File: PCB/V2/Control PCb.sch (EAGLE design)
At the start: 31 parts, among them Q1 DMP2305U-7, Q2 BSS123, Q3 BSS123, U1 V_REG_317DPACK, U2 5ACFEW

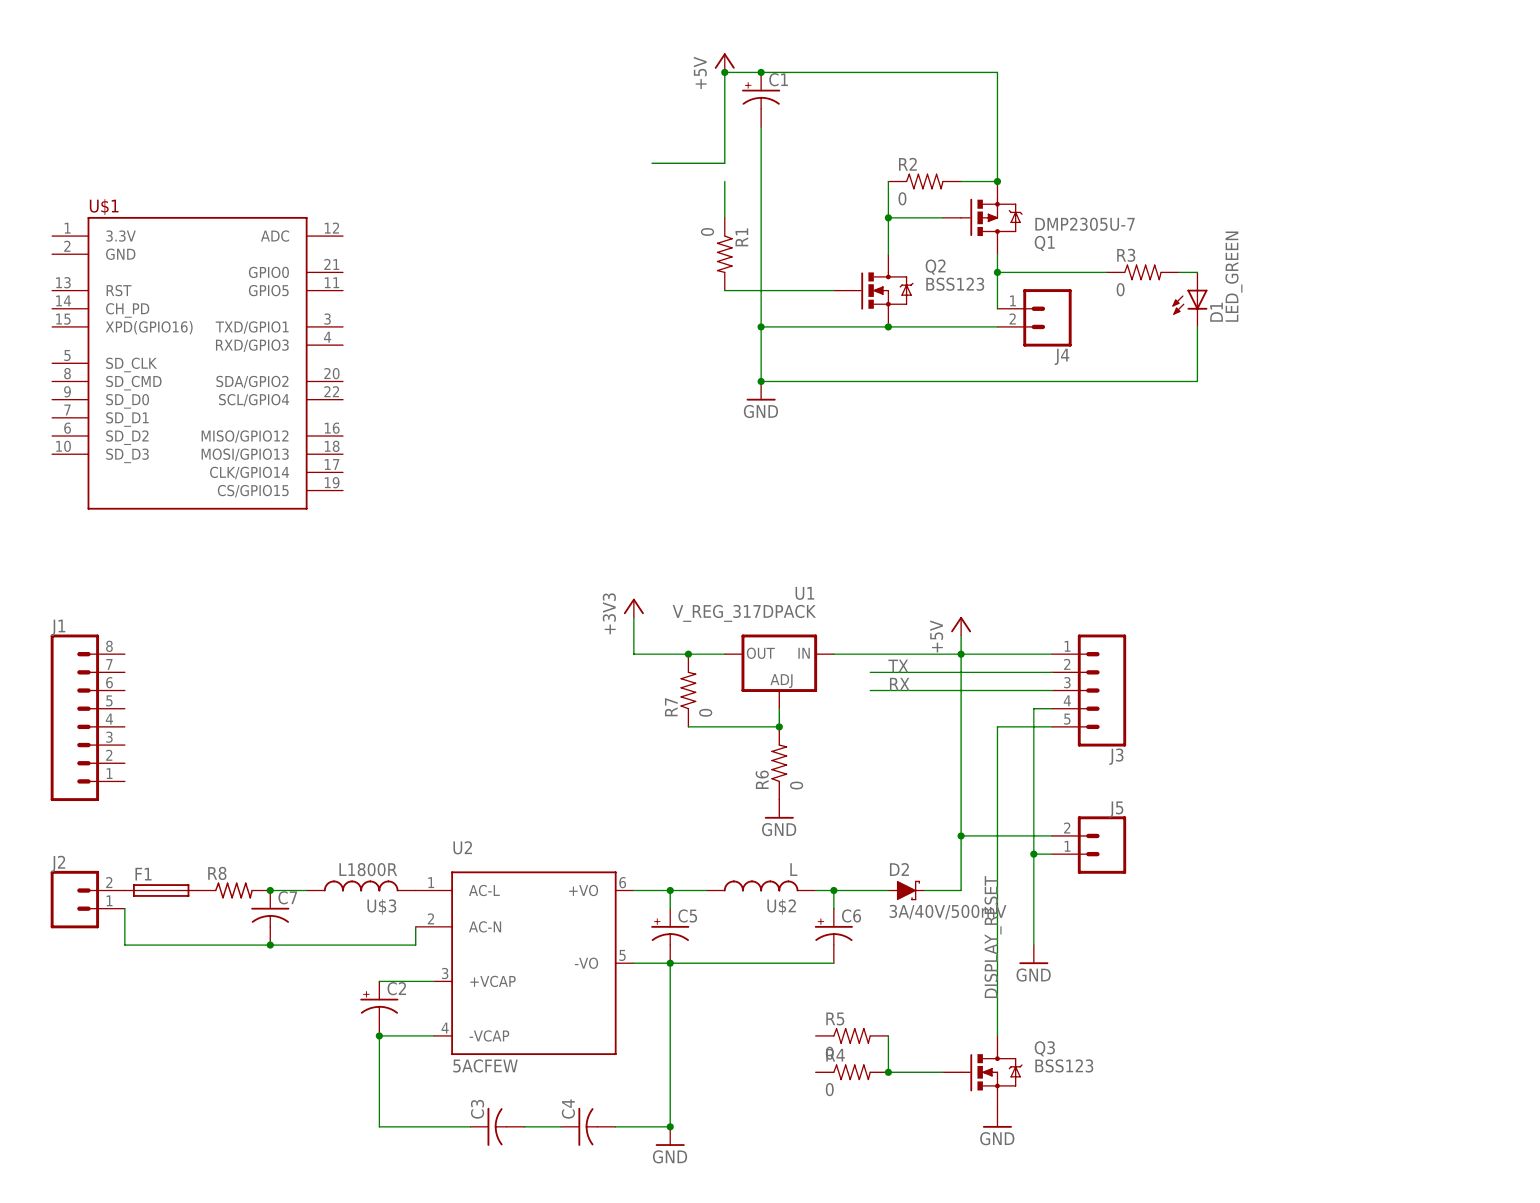
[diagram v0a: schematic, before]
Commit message: PCB + ArduinoOTA working
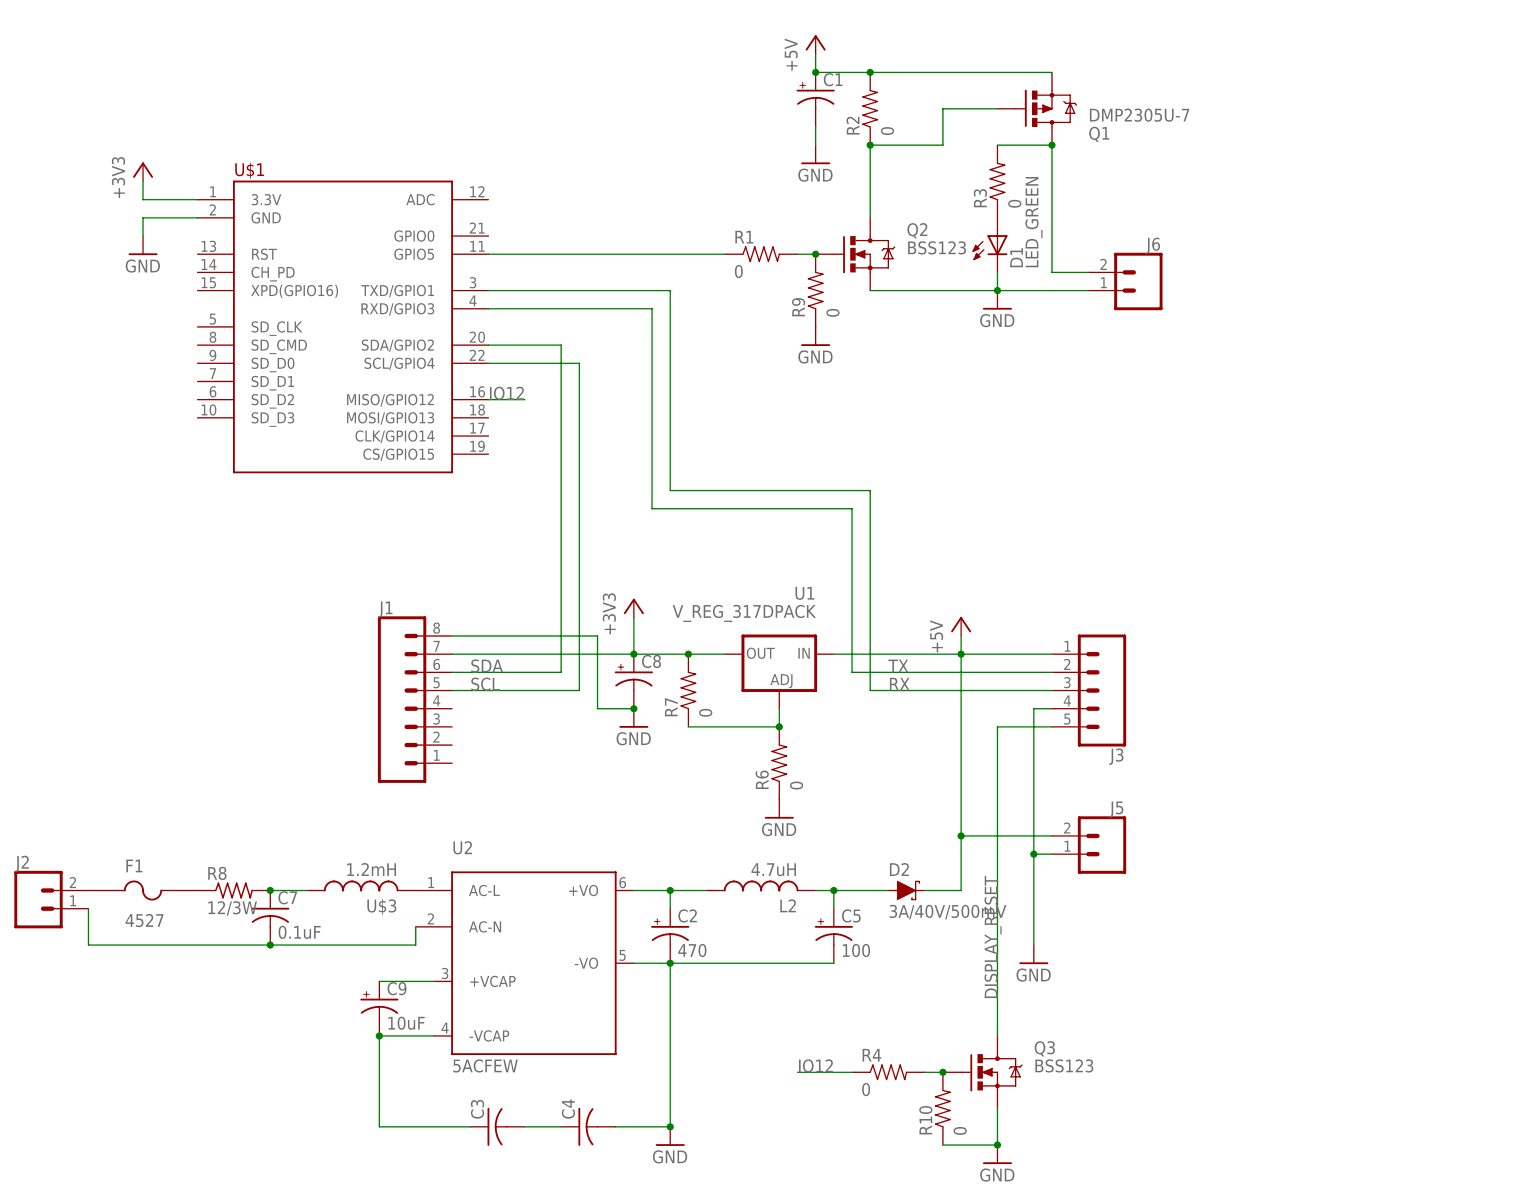
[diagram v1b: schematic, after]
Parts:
- removed C6: (no value), adafruit:CPOL-USE3.5-10
- removed J4: (no value), SparkFun-Connectors:CONN_023.5MM
- removed R5: 0, RJC-2:RES_0_0805
- added C8: (no value), adafruit:CPOL-USE2,5-6E
- added C9: 10uF, SparkFun-Capacitors:1000UF-RADIAL-5MM-35V-20%-KIT
- added J6: (no value), SparkFun-Connectors:CONN_025MM
- added R10, R9: 0, RJC-2:RES_0_0805
- C2: value (none) -> 470; device adafruit:CPOL-USE3.5-10 -> SparkFun-Capacitors:1000UF-RADIAL-5MM-35V-20%-KIT
- C5: value (none) -> 100; device adafruit:CPOL-USE3.5-10 -> SparkFun-Capacitors:1000UF-RADIAL-5MM-35V-20%-KIT
- C7: value (none) -> 0.1uF
- F1: value (none) -> 4527; device fuse:F456 -> RJC-2:4527
- L2: value L -> 4.7uH
- R8: value (none) -> 12/3W
- U$3: value L1800R -> 1.2mH
- renumbered U$2 to L2
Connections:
- new net IO12: R4.1, U$1.MISO/GPIO12
- new net SCL: J1.5, U$1.SCL/GPIO4
- new net SDA: J1.6, U$1.SDA/GPIO2
- net +3V3: now also C8.+, J1.7, U$1.3.3V
- net GND: now also C2.-, C8.-, J1.8, J6.1, R10.1, R9.1, U$1.GND; no longer C6.-, J4.2
- net N$1: now also D1.A, R3.1; no longer R1.1
- net N$10: now also F1.P$2; no longer F1.2
- net N$13: now also C9.+; no longer C2.+
- net N$14: now also C9.-; no longer C2.-
- net N$17: now also C2.+; no longer C5.+
- net N$18: now also C5.+; no longer C6.+
- net N$2: now also R9.2
- net N$3: now also F1.P$1; no longer F1.1
- net N$6: now also J6.2, R3.2; no longer J4.1, R3.1
- net N$7: now also R1.1, U$1.GPIO5; no longer D1.A, R3.2
- net N$8: now also R10.2; no longer R5.2
- net RX: now also U$1.TXD/GPIO1
- net TX: now also U$1.RXD/GPIO3
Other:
- moved on the sheet: C1, C2, C5, D1, J1, J2, Q1, Q2, R1, R2, R3, R4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

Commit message: Code + PCB stuff
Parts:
- removed J6: (no value), SparkFun-Connectors:CONN_025MM
- added D3: LED_GREEN, RJC-2:LED_GREEN
- added J4: (no value), SparkFun-Connectors:CONN_03-SCREW-5MM
- added Q4: DMP2305U-7, RJC-2:MOS-P_DMP2305U-7
- added Q5: BSS123, RJC-2:MOS-N_BSS123
- added R11, R12, R13, R5: 0, RJC-2:RES_0_0805
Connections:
- new net N$16: J4.3, Q4.D, R5.2
- new net N$19: D3.A, R5.1
- new net N$20: Q4.G, Q5.D, R11.1
- new net N$21: R13.1, U$1.MOSI/GPIO13
- new net N$22: Q5.G, R12.2, R13.2
- net +5V: now also Q4.S, R11.2
- net GND: now also D3.C, J4.2, Q5.S, R12.1; no longer J6.1
- net N$6: now also J4.1; no longer J6.2
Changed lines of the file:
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@@
 <part name="GND6" library="supply1" library_urn="urn:adsk.eagle:library:371" deviceset="GND" device=""/>
 <part name="GND7" library="supply1" library_urn="urn:adsk.eagle:library:371" deviceset="GND" device=""/>
-<part name="J6" library="SparkFun-Connectors" library_urn="urn:adsk.eagle:library:513" deviceset="CONN_02" device="5MM" package3d_urn="urn:adsk.eagle:package:38044/1"/>
 <part name="R9" library="RJC-2" library_urn="urn:adsk.eagle:library:33162582" deviceset="RES" device="_0_0805" package3d_urn="urn:adsk.eagle:package:33163805/3" value="0"/>
 <part name="GND8" library="supply1" library_urn="urn:adsk.eagle:library:371" deviceset="GND" device=""/>
@@
 <part name="C2" library="SparkFun-Capacitors" library_urn="urn:adsk.eagle:library:510" deviceset="1000UF" device="-RADIAL-5MM-35V-20%-KIT" package3d_urn="urn:adsk.eagle:package:37421/1" value="470"/>
 <part name="C5" library="SparkFun-Capacitors" library_urn="urn:adsk.eagle:library:510" deviceset="1000UF" device="-RADIAL-5MM-35V-20%-KIT" package3d_urn="urn:adsk.eagle:package:37421/1" value="100"/>
+<part name="J4" library="SparkFun-Connectors" library_urn="urn:adsk.eagle:library:513" deviceset="CONN_03" device="-SCREW-5MM" package3d_urn="urn:adsk.eagle:package:38070/1"/>
+<part name="Q4" library="RJC-2" library_urn="urn:adsk.eagle:library:33162582" deviceset="MOS-P" device="_DMP2305U-7" package3d_urn="urn:adsk.eagle:package:33163661/2" value="DMP2305U-7"/>
+<part name="R5" library="RJC-2" library_urn="urn:adsk.eagle:library:33162582" deviceset="RES" device="_0_0805" package3d_urn="urn:adsk.eagle:package:33163805/3" value="0"/>
+<part name="D3" library="RJC-2" library_urn="urn:adsk.eagle:library:33162582" deviceset="LED" device="_GREEN" package3d_urn="urn:adsk.eagle:package:33163857/2"/>
+<part name="R11" library="RJC-2" library_urn="urn:adsk.eagle:library:33162582" deviceset="RES" device="_0_0805" package3d_urn="urn:adsk.eagle:package:33163805/3" value="0"/>
+<part name="Q5" library="RJC-2" library_urn="urn:adsk.eagle:library:33162582" deviceset="MOS-N" device="_BSS123" package3d_urn="urn:adsk.eagle:package:33163661/2" value="BSS123"/>
+<part name="R12" library="RJC-2" library_urn="urn:adsk.eagle:library:33162582" deviceset="RES" device="_0_0805" package3d_urn="urn:adsk.eagle:package:33163805/3" value="0"/>
+<part name="R13" library="RJC-2" library_urn="urn:adsk.eagle:library:33162582" deviceset="RES" device="_0_0805" package3d_urn="urn:adsk.eagle:package:33163805/3" value="0"/>
+<part name="GND10" library="supply1" library_urn="urn:adsk.eagle:library:371" deviceset="GND" device=""/>
 </parts>
 <sheets>
@@
 </instance>
 <instance part="Q1" gate="G$1" x="119.38" y="96.52" smashed="yes" rot="MR180">
-<attribute name="NAME" x="124.46" y="93.98" size="1.778" layer="95" rot="MR180"/>
-<attribute name="VALUE" x="124.46" y="96.52" size="1.778" layer="96" rot="MR180"/>
+<attribute name="NAME" x="121.92" y="93.98" size="1.778" layer="95" rot="MR180"/>
+<attribute name="VALUE" x="124.46" y="91.44" size="1.778" layer="96" rot="MR270"/>
 </instance>
 <instance part="Q2" gate="G$1" x="93.98" y="76.2" smashed="yes">
@@
 <attribute name="VALUE" x="109.22" y="66.04" size="1.778" layer="96"/>
 </instance>
-<instance part="J6" gate="G$1" x="132.08" y="71.12" smashed="yes" rot="MR0">
-<attribute name="VALUE" x="134.62" y="66.294" size="1.778" layer="96" font="vector" rot="MR0"/>
-<attribute name="NAME" x="134.62" y="76.708" size="1.778" layer="95" font="vector" rot="MR0"/>
-</instance>
 <instance part="R9" gate="G$1" x="86.36" y="71.12" smashed="yes" rot="R90">
 <attribute name="NAME" x="84.8614" y="67.31" size="1.778" layer="95" rot="R90"/>
@@
 <attribute name="NAME" x="89.916" y="-17.145" size="1.778" layer="95" font="vector"/>
 <attribute name="VALUE" x="89.916" y="-21.971" size="1.778" layer="96" font="vector"/>
+</instance>
+<instance part="J4" gate="J$1" x="175.26" y="71.12" smashed="yes" rot="R180">
+<attribute name="VALUE" x="177.8" y="78.486" size="1.778" layer="96" font="vector" rot="R180"/>
+<attribute name="NAME" x="177.8" y="65.532" size="1.778" layer="95" font="vector" rot="R180"/>
+</instance>
+<instance part="Q4" gate="G$1" x="162.56" y="99.06" smashed="yes" rot="MR180">
+<attribute name="NAME" x="167.64" y="99.06" size="1.778" layer="95" rot="MR180"/>
+<attribute name="VALUE" x="167.64" y="96.52" size="1.778" layer="96" rot="MR180"/>
+</instance>
+<instance part="R5" gate="G$1" x="154.94" y="88.9" smashed="yes" rot="R90">
+<attribute name="NAME" x="153.4414" y="85.09" size="1.778" layer="95" rot="R90"/>
+<attribute name="VALUE" x="158.242" y="85.09" size="1.778" layer="96" rot="R90"/>
+</instance>
+<instance part="D3" gate="G$1" x="154.94" y="78.74" smashed="yes">
+<attribute name="NAME" x="158.496" y="76.708" size="1.778" layer="95" rot="R90"/>
+<attribute name="VALUE" x="160.655" y="76.708" size="1.778" layer="96" rot="R90"/>
+</instance>
+<instance part="R11" gate="G$1" x="147.32" y="104.14" smashed="yes" rot="R90">
+<attribute name="NAME" x="145.8214" y="100.33" size="1.778" layer="95" rot="R90"/>
+<attribute name="VALUE" x="150.622" y="100.33" size="1.778" layer="96" rot="R90"/>
+</instance>
+<instance part="Q5" gate="G$1" x="137.16" y="83.82" smashed="yes">
+<attribute name="NAME" x="142.24" y="86.36" size="1.778" layer="95"/>
+<attribute name="VALUE" x="142.24" y="83.82" size="1.778" layer="96"/>
+</instance>
+<instance part="R12" gate="G$1" x="129.54" y="55.88" smashed="yes" rot="R90">
+<attribute name="NAME" x="128.0414" y="52.07" size="1.778" layer="95" rot="R90"/>
+<attribute name="VALUE" x="132.842" y="52.07" size="1.778" layer="96" rot="R90"/>
+</instance>
+<instance part="R13" gate="G$1" x="124.46" y="60.96" smashed="yes">
+<attribute name="NAME" x="120.65" y="62.4586" size="1.778" layer="95"/>
+<attribute name="VALUE" x="120.65" y="57.658" size="1.778" layer="96"/>
+</instance>
+<instance part="GND10" gate="1" x="129.54" y="48.26" smashed="yes">
+<attribute name="VALUE" x="127" y="45.72" size="1.778" layer="96"/>
 </instance>
 </instances>
@@
 <junction x="111.76" y="71.12"/>
 <pinref part="GND7" gate="1" pin="GND"/>
-<pinref part="J6" gate="G$1" pin="1"/>
-<wire x1="124.46" y1="71.12" x2="111.76" y2="71.12" width="0.1524" layer="91"/>
+<wire x1="167.64" y1="71.12" x2="154.94" y2="71.12" width="0.1524" layer="91"/>
+<pinref part="J4" gate="J$1" pin="2"/>
+<pinref part="D3" gate="G$1" pin="C"/>
+<wire x1="154.94" y1="71.12" x2="137.16" y2="71.12" width="0.1524" layer="91"/>
+<wire x1="137.16" y1="71.12" x2="111.76" y2="71.12" width="0.1524" layer="91"/>
+<wire x1="154.94" y1="76.2" x2="154.94" y2="71.12" width="0.1524" layer="91"/>
+<junction x="154.94" y="71.12"/>
+<pinref part="Q5" gate="G$1" pin="S"/>
+<wire x1="137.16" y1="78.74" x2="137.16" y2="71.12" width="0.1524" layer="91"/>
+<junction x="137.16" y="71.12"/>
 </segment>
 <segment>
@@
 <pinref part="GND9" gate="1" pin="GND"/>
 <wire x1="-7.62" y1="81.28" x2="-7.62" y2="78.74" width="0.1524" layer="91"/>
+</segment>
+<segment>
+<pinref part="R12" gate="G$1" pin="1"/>
+<pinref part="GND10" gate="1" pin="GND"/>
 </segment>
 </net>
@@
 <wire x1="93.98" y1="101.6" x2="119.38" y2="101.6" width="0.1524" layer="91"/>
 <junction x="93.98" y="101.6"/>
+<wire x1="119.38" y1="101.6" x2="119.38" y2="109.22" width="0.1524" layer="91"/>
+<wire x1="119.38" y1="109.22" x2="147.32" y2="109.22" width="0.1524" layer="91"/>
+<junction x="119.38" y="101.6"/>
+<pinref part="Q4" gate="G$1" pin="S"/>
+<wire x1="147.32" y1="109.22" x2="162.56" y2="109.22" width="0.1524" layer="91"/>
+<wire x1="162.56" y1="109.22" x2="162.56" y2="104.14" width="0.1524" layer="91"/>
+<pinref part="R11" gate="G$1" pin="2"/>
+<junction x="147.32" y="109.22"/>
 </segment>
 <segment>
@@
 <wire x1="119.38" y1="91.44" x2="119.38" y2="73.66" width="0.1524" layer="91"/>
 <junction x="119.38" y="91.44"/>
-<pinref part="J6" gate="G$1" pin="2"/>
-<wire x1="119.38" y1="73.66" x2="124.46" y2="73.66" width="0.1524" layer="91"/>
+<wire x1="119.38" y1="73.66" x2="167.64" y2="73.66" width="0.1524" layer="91"/>
+<pinref part="J4" gate="J$1" pin="1"/>
 </segment>
 </net>
@@
 </segment>
 </net>
+<net name="N$16" class="0">
+<segment>
+<pinref part="Q4" gate="G$1" pin="D"/>
+<wire x1="162.56" y1="93.98" x2="162.56" y2="68.58" width="0.1524" layer="91"/>
+<pinref part="J4" gate="J$1" pin="3"/>
+<wire x1="162.56" y1="68.58" x2="167.64" y2="68.58" width="0.1524" layer="91"/>
+<pinref part="R5" gate="G$1" pin="2"/>
+<wire x1="154.94" y1="93.98" x2="162.56" y2="93.98" width="0.1524" layer="91"/>
+<junction x="162.56" y="93.98"/>
+</segment>
+</net>
+<net name="N$19" class="0">
+<segment>
+<pinref part="R5" gate="G$1" pin="1"/>
+<pinref part="D3" gate="G$1" pin="A"/>
+</segment>
+</net>
+<net name="N$20" class="0">
+<segment>
+<pinref part="R11" gate="G$1" pin="1"/>
+<pinref part="Q4" gate="G$1" pin="G"/>
+<wire x1="147.32" y1="99.06" x2="154.94" y2="99.06" width="0.1524" layer="91"/>
+<pinref part="Q5" gate="G$1" pin="D"/>
+<wire x1="137.16" y1="88.9" x2="137.16" y2="99.06" width="0.1524" layer="91"/>
+<wire x1="137.16" y1="99.06" x2="147.32" y2="99.06" width="0.1524" layer="91"/>
+<junction x="147.32" y="99.06"/>
+</segment>
+</net>
+<net name="N$22" class="0">
+<segment>
+<pinref part="R12" gate="G$1" pin="2"/>
+<pinref part="R13" gate="G$1" pin="2"/>
+<pinref part="Q5" gate="G$1" pin="G"/>
+<wire x1="129.54" y1="83.82" x2="129.54" y2="60.96" width="0.1524" layer="91"/>
+<junction x="129.54" y="60.96"/>
+</segment>
+</net>
+<net name="N$21" class="0">
+<segment>
+<pinref part="U$1" gate="G$1" pin="MOSI/GPIO13"/>
+<wire x1="40.64" y1="53.34" x2="111.76" y2="53.34" width="0.1524" layer="91"/>
+<wire x1="111.76" y1="53.34" x2="111.76" y2="60.96" width="0.1524" layer="91"/>
+<pinref part="R13" gate="G$1" pin="1"/>
+<wire x1="111.76" y1="60.96" x2="119.38" y2="60.96" width="0.1524" layer="91"/>
+</segment>
+</net>
